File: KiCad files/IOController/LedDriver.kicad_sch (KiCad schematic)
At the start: 31 parts, among them IC1 TPS923654DMTR

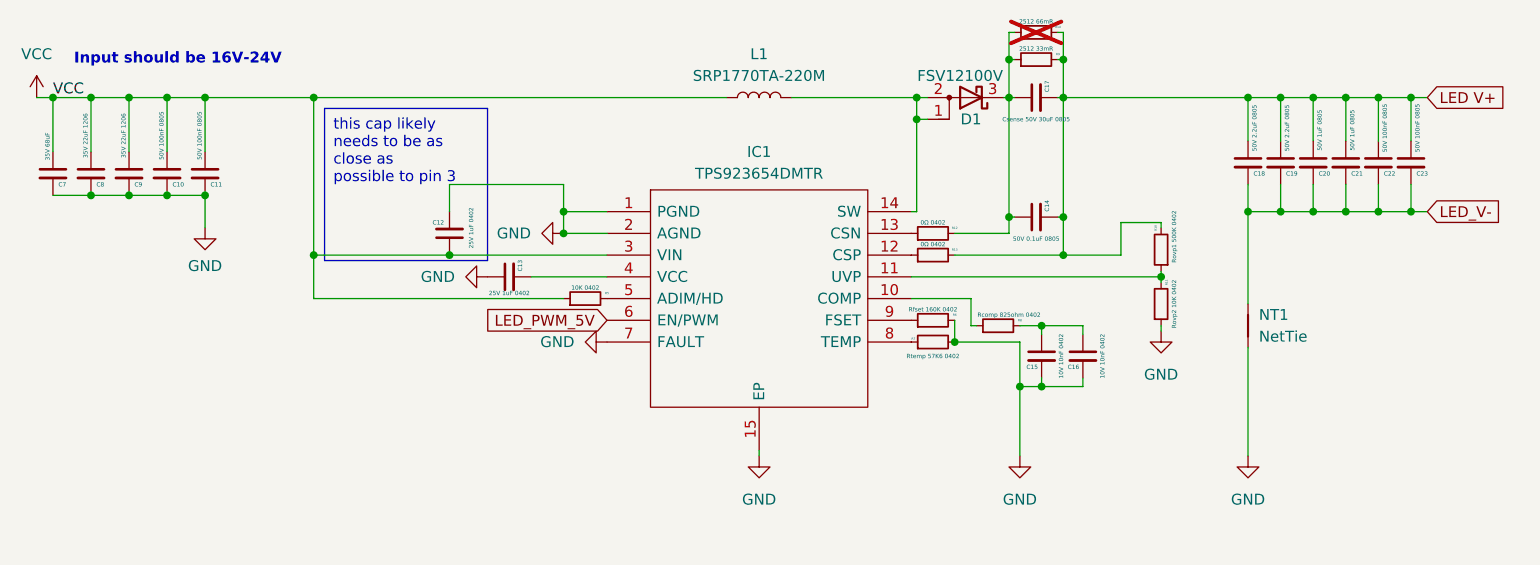
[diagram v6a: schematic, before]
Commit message: modified design to be closer to reference version.
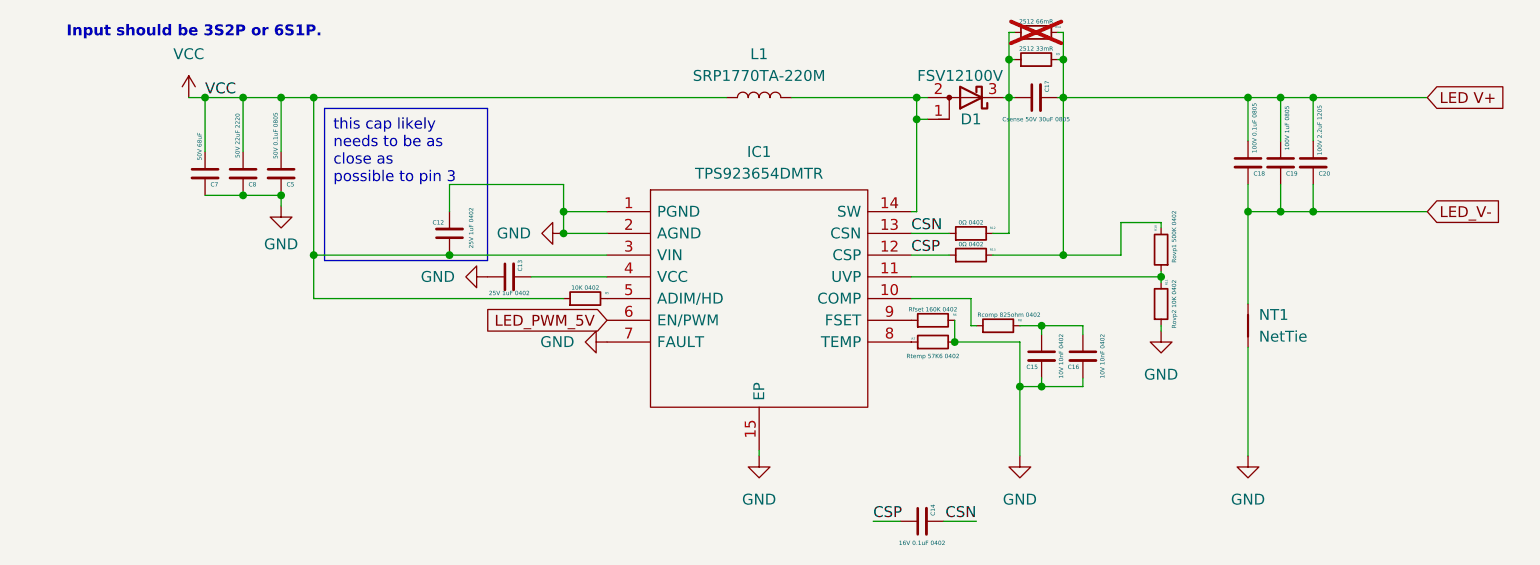
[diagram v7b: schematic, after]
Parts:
- removed C10, C11, C22, C23: 50V 100nF 0805, Capacitor_SMD:C_0805_2012Metric, symbol Device:C_Small
- removed C21: 50V 1uF 0805, Capacitor_SMD:C_0805_2012Metric, symbol Device:C_Small
- removed C9: 35V 22uF 1206, Capacitor_SMD:C_1206_3216Metric, symbol Device:C_Small
- added C5: 50V 0.1uF 0805, Capacitor_SMD:C_0805_2012Metric, symbol Device:C_Small
- C14: value 50V 0.1uF 0805 -> 16V 0.1uF 0402; footprint Capacitor_SMD:C_0805_2012Metric -> Capacitor_SMD:C_0402_1005Metric
- C18: value 50V 2.2uF 0805 -> 100V 0.1uF 0805
- C19: value 50V 2.2uF 0805 -> 100V 1uF 0805
- C20: value 50V 1uF 0805 -> 100V 2.2uF 1205; footprint Capacitor_SMD:C_0805_2012Metric -> Capacitor_SMD:C_1206_3216Metric
- C7: value 35V 68uF -> 50V 68uF; footprint Capacitor_Tantalum_SMD:CP_EIA-7343-43_Kemet-X -> Capacitor_SMD:CP_Elec_6.3x3
- C8: value 35V 22uF 1206 -> 50V 22uF 2220; footprint Capacitor_SMD:C_1206_3216Metric -> Capacitor_SMD:C_2220_5750Metric
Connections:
- net GND: now also C5.2
- net LED V+: no longer C14.2
- net VCC: now also C5.1
- net CSP: now reaches IC1.12 (CSP), R13.1
- net CSP: now also C14.1
- net at C17.1, D1.3 (K), R12.2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: no longer C14.1
- net CSN: now reaches IC1.13 (CSN), R12.1
- net CSN: now also C14.2
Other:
- note added: "Input should be 3S2P or 6S1P."
- note removed: "Input should be 16V-24V"
- moved on the sheet: C14, C7, C8, R12, R13

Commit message: corrected a few things to make life a bit easier.
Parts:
- IC1: footprint TPS922054DMTR:SON65P300X450X100-15N-D -> Package_SON:VSON-14-1EP_3x4.45mm_P0.65mm_EP1.6x4.2mm_ThermalVias
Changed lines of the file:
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@@
 			)
 		)
-		(property "Footprint" "TPS922054DMTR:SON65P300X450X100-15N-D"
+		(property "Footprint" "Package_SON:VSON-14-1EP_3x4.45mm_P0.65mm_EP1.6x4.2mm_ThermalVias"
 			(at 119.38 56.515 0)
 			(effects
